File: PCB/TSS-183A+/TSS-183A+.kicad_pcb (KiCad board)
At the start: 4 copper layers, 55.3 x 35 mm, 25 parts, among them U1 TSS-183A+, U2 L7805

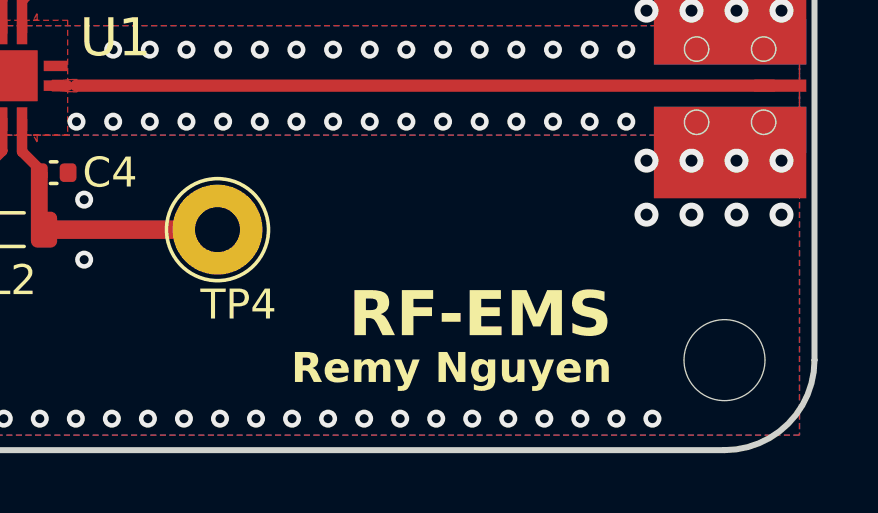
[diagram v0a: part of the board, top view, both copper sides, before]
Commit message: pcb: added boms, updated readmes, changed silkscreen from dfs/ems to nmsm
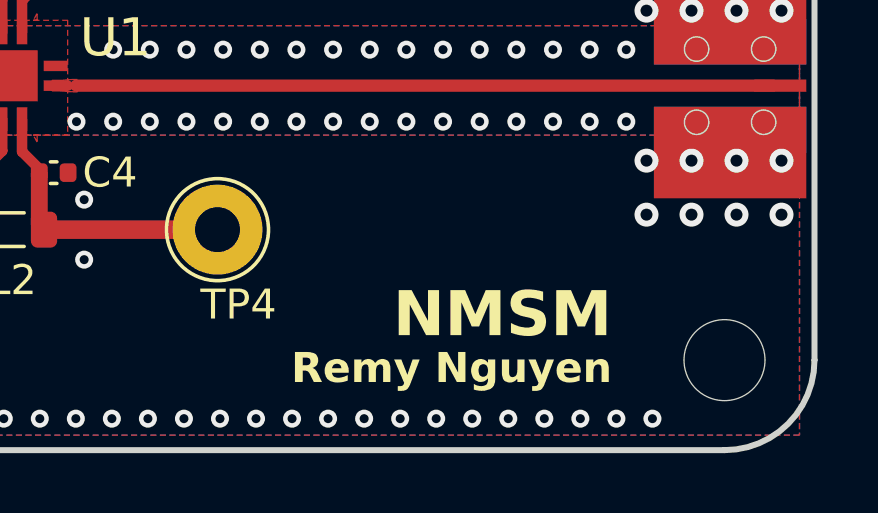
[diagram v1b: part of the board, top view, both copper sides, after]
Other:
- board text added: "NMSM"
- board text removed: "RF-EMS"
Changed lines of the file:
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@@
     (effects (font (size 1 1) (thickness 0.2) bold) (justify left bottom mirror))
   )
-  (gr_text "RF-EMS" (at 159.35 102.5) (layer "F.SilkS")
+  (gr_text "NMSM" (at 159.35 102.5) (layer "F.SilkS")
     (effects (font (size 1.5 1.5) (thickness 0.3) bold) (justify right bottom))
   )

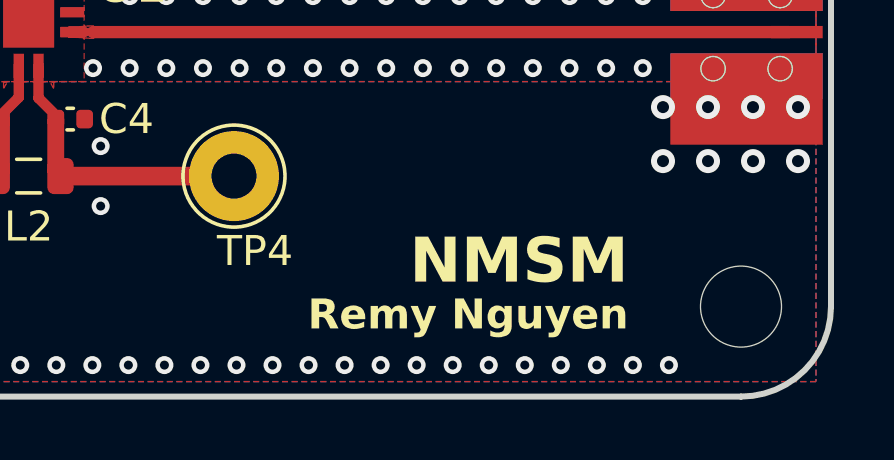
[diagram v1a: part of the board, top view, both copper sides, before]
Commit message: pcb: fixed silkscreen to be consistent with pma3-14ln+ (name, revision, device)
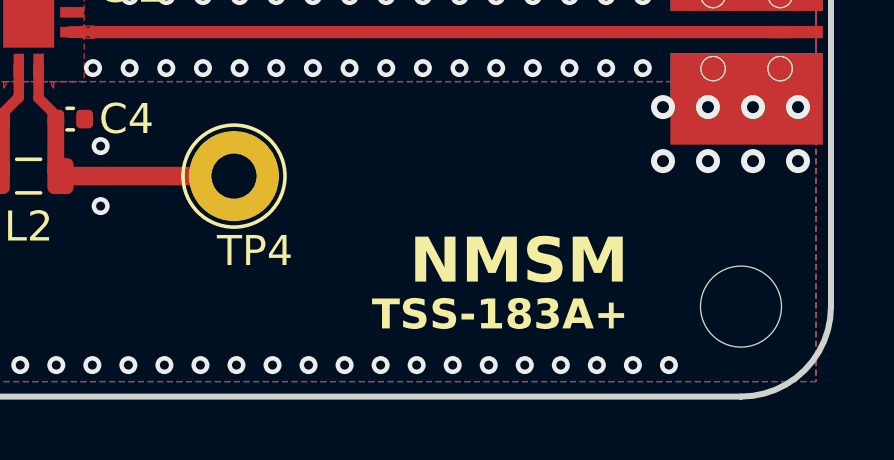
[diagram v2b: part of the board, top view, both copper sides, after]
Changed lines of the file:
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@@
   (gr_line (start 128.45 88.56) (end 128.45 88.74)
     (stroke (width 0.2) (type solid)) (layer "User.9"))
-  (gr_text "TSS-183A+" (at 159.35 104) (layer "B.SilkS")
+  (gr_text "Remy Nguyen" (at 159.35 104) (layer "B.SilkS")
     (effects (font (size 1 1) (thickness 0.2) bold) (justify left bottom mirror))
   )
@@
     (effects (font (size 1.5 1.5) (thickness 0.3) bold) (justify right bottom))
   )
-  (gr_text "Remy Nguyen" (at 159.35 104) (layer "F.SilkS")
+  (gr_text "TSS-183A+" (at 159.35 104) (layer "F.SilkS")
     (effects (font (size 1 1) (thickness 0.2) bold) (justify right bottom))
   )

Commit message: pcb: fixed 3d model references for connectors and mmic componenets
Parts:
- RF-In, RF-Out: footprint footprints:Mueller BU-1420761881 -> rf-dfs:Mueller BU-1420761881
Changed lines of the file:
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@@
     (pad "9" smd rect (at 0 0) (size 1.702 1.702) (layers "F.Cu" "F.Paste" "F.Mask")
       (net 4 "GND") (pinfunction "EP") (pintype "passive"))
-    (model "TSS-183A+.stp"
+    (model "${KIPRJMOD}/../_dependencies/3dmodels/TSS-183A+.stp"
       (offset (xyz 0 0 0))
       (scale (xyz 1 1 1))
@@
     )
   )
-  (footprint "footprints:Mueller BU-1420761881" (layer "F.Cu")
+  (footprint "rf-dfs:Mueller BU-1420761881" (layer "F.Cu")
     (at 161.56 94 180)
     (descr "Molex SMA RF Connectors, Edge Mount, (http://www.molex.com/pdm_docs/sd/732511150_sd.pdf)")
@@
     (pad "2" smd rect (at -1.7272 2.2292 180) (size 5.08 3.048) (layers "F.Cu" "F.Paste" "F.Mask")
       (net 4 "GND") (pinfunction "Ext") (pintype "passive"))
-    (model "C:/Users/remyv/Documents/KiCad/7.0/3dmodels/BU-1420761881.stp"
-      (offset (xyz -14.097 0 0))
+    (model "${KIPRJMOD}/../_dependencies/3dmodels/BU-1420761881.stp"
+      (offset (xyz -14.22 0 0.22))
       (scale (xyz 1 1 1))
       (rotate (xyz 0 0 180))
@@
     )
   )
-  (footprint "footprints:Mueller BU-1420761881" (layer "F.Cu")
+  (footprint "rf-dfs:Mueller BU-1420761881" (layer "F.Cu")
     (at 115.39 94)
     (descr "Molex SMA RF Connectors, Edge Mount, (http://www.molex.com/pdm_docs/sd/732511150_sd.pdf)")
@@
     (pad "2" smd rect (at -1.7272 2.2292) (size 5.08 3.048) (layers "F.Cu" "F.Paste" "F.Mask")
       (net 4 "GND") (pinfunction "Ext") (pintype "passive"))
-    (model "C:/Users/remyv/Documents/KiCad/7.0/3dmodels/BU-1420761881.stp"
-      (offset (xyz -14.097 0 0))
+    (model "${KIPRJMOD}/../_dependencies/3dmodels/BU-1420761881.stp"
+      (offset (xyz -14.22 0 0.22))
       (scale (xyz 1 1 1))
       (rotate (xyz 0 0 180))
